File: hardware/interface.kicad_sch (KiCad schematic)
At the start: 0 parts

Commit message: Interface sheet: 2068 bus transceivers, gating, open-drain drivers, DMA drivers
- lib/tspico.kicad_sym: TS2068_Edge symbol (A1..A32/B1..B32, manual pin names)
- scripts/schlib.py: small KiCad schematic writer (stock symbols embedded
  verbatim, labels on pins, grid-snapped placement)
- scripts/gen_interface.py: P1, 4x 74LVC245, 74LVC04/08 gating, 74LVC07
  open-drain, 74LVC126 DMA drivers, 74LVC1G86 data direction, buttons,
  reset pull-down, EAR divider, decoupling
- Power decision: +5V from the edge only, USB is data only
- ERC: only cross-sheet labels remain (isolated/undriven until other sheets exist)

Co-Authored-By: Claude Fable 5.1 <noreply@anthropic.com>
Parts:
- added C1, C2, C3, C4, C5, C6, C7, C8: 100n, Capacitor_SMD:C_0603_1608Metric, symbol Device:C
- added P1: TS2068_Edge, tspico:TS2068_EdgeConnector_2x32, symbol tspico:TS2068_Edge
- added R1: 10k, Resistor_SMD:R_0603_1608Metric, symbol Device:R
- added R2: 4k7, Resistor_SMD:R_0603_1608Metric, symbol Device:R
- added R3: 1k, Resistor_SMD:R_0603_1608Metric, symbol Device:R
- added SW1: TS Reset, Button_Switch_SMD:SW_SPST_PTS645Sx43SMTR92, symbol Switch:SW_Push
- added SW2: NMI, Button_Switch_SMD:SW_SPST_PTS645Sx43SMTR92, symbol Switch:SW_Push
- added U1, U2, U3, U4: 74LVC245APW, Package_SO:TSSOP-20_4.4x6.5mm_P0.65mm, symbol 74xx:74LS245
- added U5: 74LVC04APW, Package_SO:TSSOP-14_4.4x5mm_P0.65mm, symbol 74xx:74LS04
- added U6: 74LVC08APW, Package_SO:TSSOP-14_4.4x5mm_P0.65mm, symbol 74xx:74LS08
- added U7: 74LVC07APW, Package_SO:TSSOP-14_4.4x5mm_P0.65mm, symbol 74xx:74LS07
- added U8: 74LVC126APW, Package_SO:TSSOP-14_4.4x5mm_P0.65mm, symbol 74xx:74LS126
- added U9: 74LVC1G86, Package_TO_SOT_SMD:SOT-23-5, symbol 74xGxx:74LVC1G86
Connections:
- new net +3V3: C1.1, C2.1, C3.1, C4.1, C5.1, C6.1, C7.1, C8.1, U1.20 (VCC), U2.20 (VCC), U3.20 (VCC), U4.20 (VCC), U5.14 (VCC), U6.14 (VCC), U7.13, U7.14 (VCC), U8.14 (VCC), U9.5 (VCC)
- new net +5V: P1.B4 (+5V)
- new net A0: P1.B10 (A0), U1.18 (B0)
- new net A1: P1.B11 (A1), U1.17 (B1)
- new net A10: P1.B19 (A10), U2.16 (B2)
- new net A11: P1.B18 (A11), U2.15 (B3)
- new net A12: P1.B17 (A12), U2.14 (B4)
- new net A13: P1.B16 (A13), U2.13 (B5)
- new net A14: P1.B15 (A14), U2.12 (B6), U4.13 (B5)
- new net A15: P1.B14 (A15), U2.11 (B7), U4.12 (B6)
- new net A2: P1.B12 (A2), U1.16 (B2)
- new net A3: P1.B13 (A3), U1.15 (B3)
- new net A4: P1.B25 (A4), U1.14 (B4)
- new net A5: P1.B24 (A5), U1.13 (B5)
- new net A6: P1.B23 (A6), U1.12 (B6)
- new net A7: P1.B22 (A7), U1.11 (B7)
- new net A8: P1.B21 (A8), U2.18 (B0)
- new net A9: P1.B20 (A9), U2.17 (B1)
- new net BUS_OWN: U6.12
- new net D0: P1.A7 (D0), U3.2 (A0)
- new net D1: P1.A8 (D1), U3.3 (A1)
- new net D2: P1.A9 (D2), U3.4 (A2)
- new net D3: P1.A12 (D3), U3.5 (A3)
- new net D4: P1.A13 (D4), U3.6 (A4)
- new net D5: P1.A11 (D5), U3.7 (A5)
- new net D6: P1.A10 (D6), U3.8 (A6)
- new net D7: P1.A4 (D7), U3.9 (A7)
- new net DATA_DIR: U3.1 (A->B), U9.4
- new net DMA_A14: U2.8 (A6)
- new net DMA_A15: U2.9 (A7)
- new net DMA_EN: U1.1 (A->B), U2.1 (A->B), U5.11, U8.1, U8.10, U8.4, U9.2
- new net EAR: P1.A2 (EAR), R2.2, R3.1
- new net GND: C1.2, C2.2, C3.2, C4.2, C5.2, C6.2, C7.2, C8.2, P1.A1 (GND), P1.A32 (GND), P1.B1 (GND), P1.B32 (GND), P1.B7 (PGND), P1.B8 (PGND), R1.2, R3.2, SW1.2, SW2.2, U1.10 (GND), U2.10 (GND), U3.10 (GND), U4.1 (A->B), U4.10 (GND), U4.19 (CE), U5.13, U5.7 (GND), U6.7 (GND), U7.7 (GND), U8.12, U8.13, U8.7 (GND), U9.3 (GND)
- new net IORQ_H: U5.4, U6.4
- new net IORQ_M1: U5.9, U6.6
- new net MA0: U1.2 (A0)
- new net MA1: U1.3 (A1)
- new net MA10: U2.4 (A2)
- new net MA11: U2.5 (A3)
- new net MA12: U2.6 (A4)
- new net MA13: U2.7 (A5)
- new net MA2: U1.4 (A2)
- new net MA3: U1.5 (A3)
- new net MA4: U1.6 (A4)
- new net MA5: U1.7 (A5)
- new net MA6: U1.8 (A6)
- new net MA7: U1.9 (A7)
- new net MA8: U2.2 (A0)
- new net MA9: U2.3 (A1)
- new net MD0: U3.18 (B0)
- new net MD1: U3.17 (B1)
- new net MD2: U3.16 (B2)
- new net MD3: U3.15 (B3)
- new net MD4: U3.14 (B4)
- new net MD5: U3.13 (B5)
- new net MD6: U3.12 (B6)
- new net MD7: U3.11 (B7)
- new net MREQ_H: U5.2, U6.1
- new net MREQ_RFSH: U5.5, U6.3
- new net RESET_REQ: R1.1, U7.11
- new net SOUND_2068: P1.A31 (SOUND)
- new net SPKR_TAPE: P1.B2 (SPKR_TAPE), U4.11 (B7)
- new net TAPE_IN: U4.9 (A7)
- new net TAPE_OUT: R2.1
- new net Z80_A14: U4.7 (A5)
- new net Z80_A15: U4.8 (A6)
- new net nBE: P1.A29 (~{BE}), U7.2
- new net nBE_G: U7.1
- new net nBUSAK: P1.A21 (~{BUSAK})
- new net nBUSRQ: P1.A23 (~{BUSRQ}), U7.6
- new net nBUSRQ_G: U7.5
- new net nDATA_OE: U3.19 (CE)
- new net nDMA_EN: U5.10, U6.13
- new net nDMA_MREQ: U6.8, U8.2
- new net nEXROM: P1.A27 (~{EXROM}), U4.15 (B3)
- new net nEXROM_L: U4.5 (A3)
- new net nINT: P1.A14 (~{INT}), U4.14 (B4)
- new net nINT_L: U4.6 (A4)
- new net nIORQ: P1.A18 (~{IORQ}), U5.3
- new net nIORQ_V: U5.8
- new net nM1: P1.A25 (~{M1}), U6.5
- new net nMRD: U6.9, U8.5
- new net nMREQ: P1.A17 (~{MREQ}), U5.1, U8.3
- new net nMREQ_V: U5.6
- new net nMWR: U6.10, U8.9
- new net nNMI: P1.A15 (~{NMI}), SW2.1, U7.8
- new net nNMI_G: U7.9
- new net nOE_ADDR: U1.19 (CE), U2.19 (CE), U6.11
- new net nRD: P1.A19 (~{RD}), U4.18 (B0), U8.6, U9.1
- new net nRD_L: U4.2 (A0)
- new net nRESET: P1.A24 (~{RESET}), SW1.1, U7.10
- new net nRFSH: P1.A26 (~{RFSH}), U6.2
- new net nROSCS: P1.A28 (~{ROSCS}), U4.16 (B2)
- new net nROSCS_L: U4.4 (A2)
- new net nWAIT: P1.A22 (~{WAIT}), U7.4
- new net nWAIT_G: U7.3
- new net nWR: P1.A20 (~{WR}), U4.17 (B1), U8.8
- new net nWR_L: U4.3 (A1)
- no-connect marks 0 -> 16
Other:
- note added: "Power: +5V from edge pin B4 only. +15V (B3) unused. USB is data only."
- note added: "R2/R3: TAPE_OUT (3.3 V) divided to about 0.6 V for the 2068 EAR input; values to be confirmed on the prototype."
- note added: "TS2068 bus interface. Nets: n = active low, _L = 3.3 V copy of a bus signal, _G = 3.3 V request driven onto the bus through an open-drain buffer."
- note removed: "Edge connector, address/data/control transceivers, open-drain drivers, reset, buttons, tape EAR/MIC dividers"

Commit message: Interface sheet: fix symbol text placement and layout overlaps
Co-Authored-By: Claude Fable 5.1 <noreply@anthropic.com>
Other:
- note added: "R2/R3: TAPE_OUT divided to ~0.6 V for the 2068 EAR input."
- note added: "Values to be confirmed on the prototype."
- note removed: "R2/R3: TAPE_OUT (3.3 V) divided to about 0.6 V for the 2068 EAR input; values to be confirmed on the prototype."

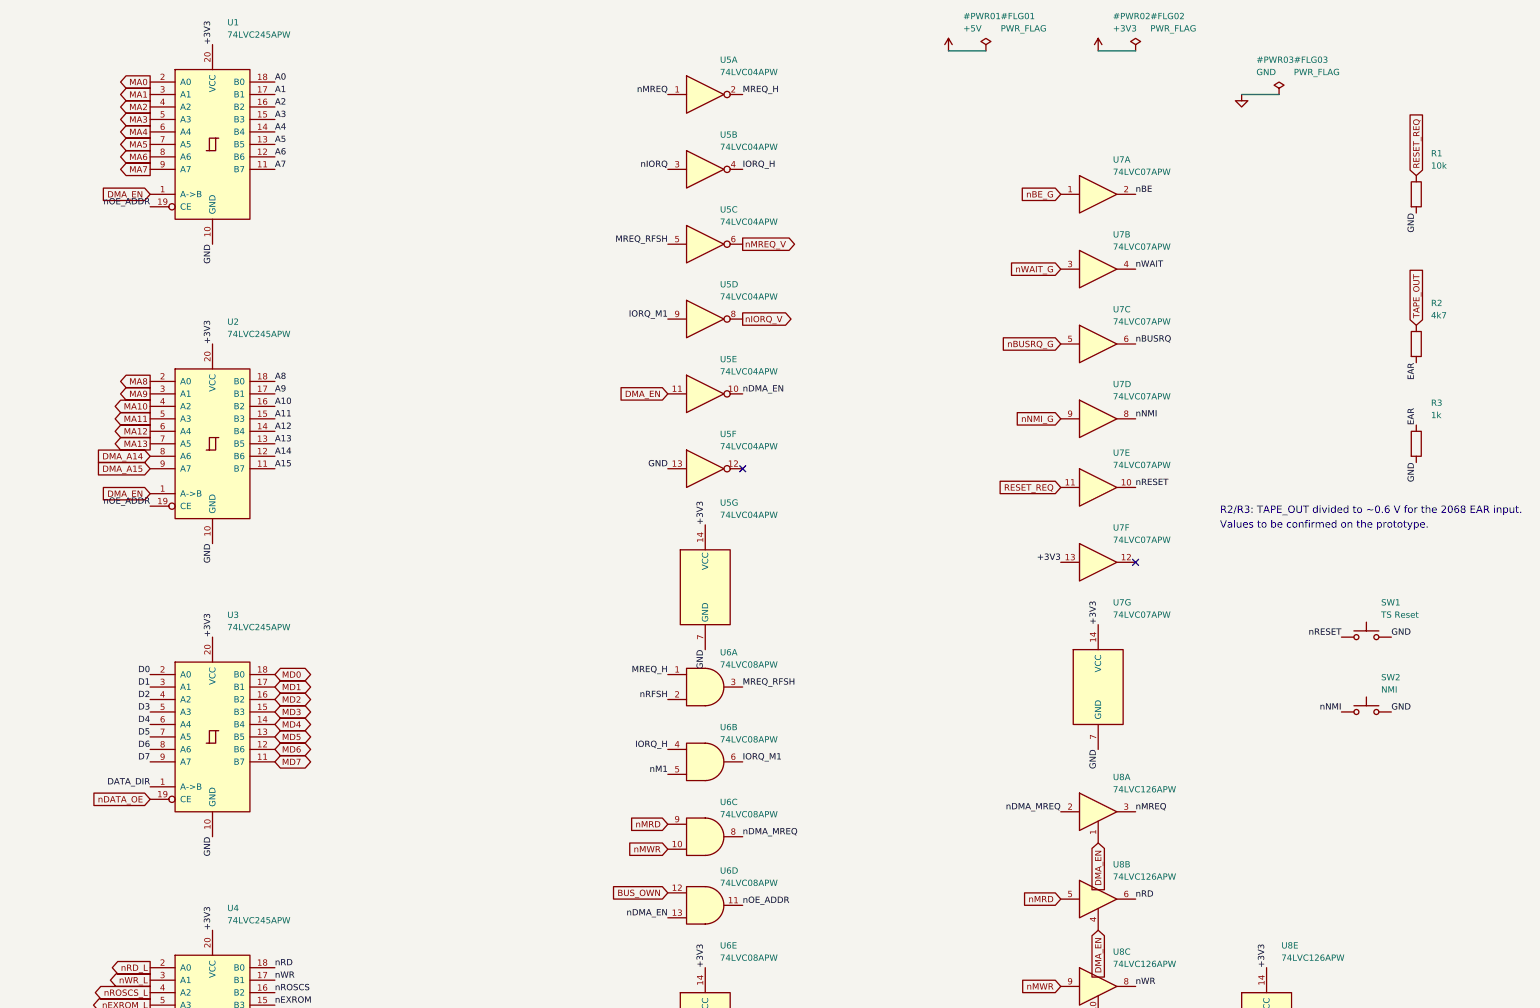
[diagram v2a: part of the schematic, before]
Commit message: Emulated memory: rewrite architecture, add local-bus/register sheet
- docs/v3-architecture.md: RP2350B serves DCK/ROM images from internal SRAM
  via PIO+DMA; no flash or SRAM chips; 8-bit multiplexed local bus; slot map
  file replaces fixed flash banks; ESP32-C3-WROOM-02 for Zimodem.
- memory sheet: 74LVC257 address byte muxes, ALO/AHI/CTL/STAT registers,
  74LVC139 select, power-on clear for CTL.
- interface sheet: 74LVC06 inverting open-drain drivers with active-high
  requests (safe power-up state), RESET_HOLD pull-up, address transceivers
  always enabled, MA8-MA15 to the muxes, WIFI_DL inverter.
- ERC: only cross-sheet labels/inputs pending the MCU and peripheral sheets.

Co-Authored-By: Claude Fable 5.1 <noreply@anthropic.com>
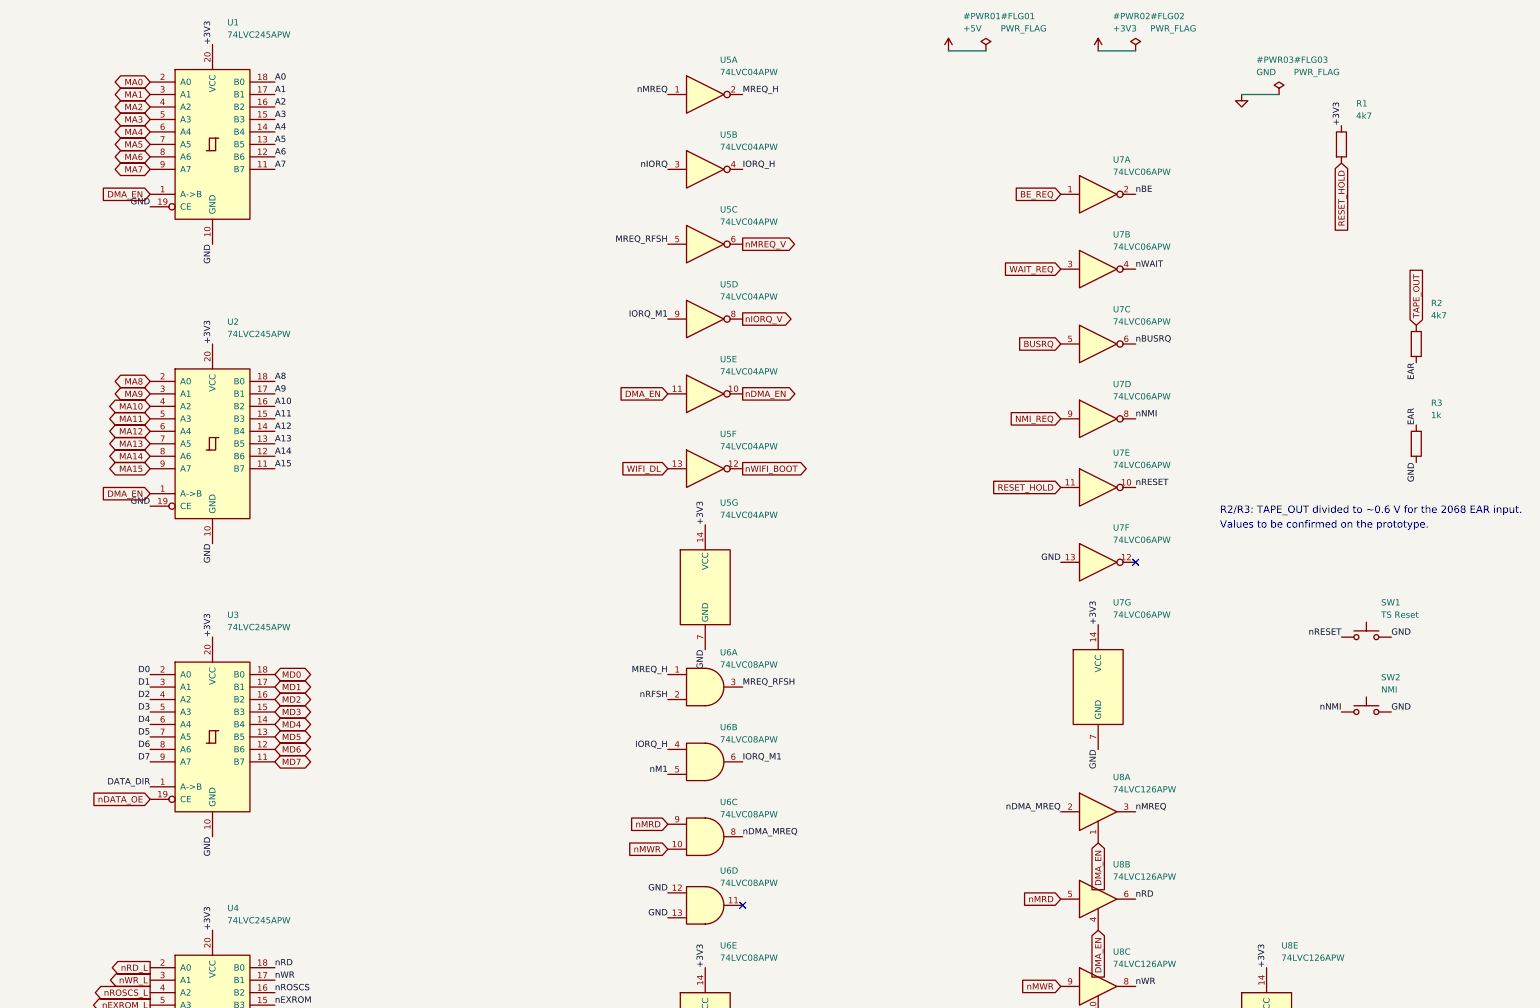
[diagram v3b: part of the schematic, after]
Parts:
- removed U7: 74LVC07APW, Package_SO:TSSOP-14_4.4x5mm_P0.65mm, symbol 74xx:74LS07
- added U7: 74LVC06APW, Package_SO:TSSOP-14_4.4x5mm_P0.65mm, symbol 74xx:74LS06
- R1: value 10k -> 4k7
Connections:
- net BUS_OWN is gone; now on net GND: U6.12
- net RESET_REQ is gone; now on net +3V3: R1.1
- net +3V3: now also U7.14 (VCC)
- net GND: now also U1.19 (CE), U2.19 (CE), U6.13, U7.13, U7.7 (GND); no longer R1.2, U5.13
- net nBE: now also U7.2
- net nBUSRQ: now also U7.6
- net nDMA_EN: no longer U6.13
- net nNMI: now also U7.8
- net nRESET: now also U7.10
- net nWAIT: now also U7.4
- net nWIFI_BOOT: now reaches U5.12
- net DMA_A14 renamed MA14
- net DMA_A15 renamed MA15
- removed net nOE_ADDR: U1.19 (CE), U2.19 (CE), U6.11
- new net BE_REQ: U7.1
- new net BUSRQ: U7.5
- new net NMI_REQ: U7.9
- new net RESET_HOLD: R1.2, U7.11
- new net WAIT_REQ: U7.3
- new net WIFI_DL: U5.13

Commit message: Remaining sheets: power, SD and display, WiFi, audio, joystick; ERC clean
- Power: Schottky diode-OR of edge +5V and USB VBUS (card runs from the
  2068/expansion bus, USB alone, or both), two TLV1117LV33 LDOs, bulk caps
- SD: Hirose DM3AT in SPI mode with series R, pull-ups, card detect to STAT
- OLED: 7-pin header (Waveshare 1.27in 128x96 SSD1351) on SPI1
- WiFi: ESP32-C3-WROOM-02 on UART, EN/boot from CTL, IO8 pull-up
- Audio: PWM low-pass, 2068 SOUND mix, MCP6002 buffers, 3.5 mm jack
- Joystick: DE-9 Kempston with pull-ups, series R, optional +5V jumper
- Memory sheet: activity LED on CTL bit 6
- Docs: power decision updated

Co-Authored-By: Claude Fable 5.1 <noreply@anthropic.com>
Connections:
- net +5V renamed +5V_EDGE
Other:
- note added: "Power: edge +5V (B4) goes to the power sheet as +5V_EDGE and is diode-ORed with USB VBUS. +15V (B3) unused."
- note removed: "Power: +5V from edge pin B4 only. +15V (B3) unused. USB is data only."
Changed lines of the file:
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@@
   (title_block (title "TS-Pico v3: 2068 Interface") (rev "0.1") (company "Timex/Sinclair Online User Group"))
   (text "TS2068 bus interface. Nets: n = active low, _L = 3.3 V copy of a bus signal, _G = 3.3 V request driven onto the bus through an open-drain buffer." (exclude_from_sim no) (at 20 285 0) (effects (font (size 2.5 2.5)) (justify left bottom)))
-  (text "Power: +5V from edge pin B4 only. +15V (B3) unused. USB is data only." (exclude_from_sim no) (at 20 290 0) (effects (font (size 2.0 2.0)) (justify left bottom)))
+  (text "Power: edge +5V (B4) goes to the power sheet as +5V_EDGE and is diode-ORed with USB VBUS. +15V (B3) unused." (exclude_from_sim no) (at 20 290 0) (effects (font (size 2.0 2.0)) (justify left bottom)))
   (symbol (lib_id "tspico:TS2068_Edge") (at 59.69 119.38 0) (unit 1)
     (exclude_from_sim no) (in_bom yes) (on_board yes) (dnp no)
@@
   (label "GND" (at 77.47 95.25 0) (effects (font (size 1.27 1.27)) (justify left bottom)))
   (label "GND" (at 77.47 97.79 0) (effects (font (size 1.27 1.27)) (justify left bottom)))
-  (label "+5V" (at 77.47 87.63 0) (effects (font (size 1.27 1.27)) (justify left bottom)))
+  (global_label "+5V_EDGE" (shape output) (at 77.47 87.63 0) (effects (font (size 1.27 1.27)) (justify left)))
   (label "EAR" (at 41.91 82.55 180) (effects (font (size 1.27 1.27)) (justify right bottom)))
   (label "SPKR_TAPE" (at 77.47 82.55 0) (effects (font (size 1.27 1.27)) (justify left bottom)))
@@
   (no_connect (at 77.47 153.67))
   (no_connect (at 77.47 156.21))
-  (symbol (lib_id "power:+5V") (at 299.72 30.48 0) (unit 1)
-    (exclude_from_sim no) (in_bom yes) (on_board yes) (dnp no)
-    (property "Reference" "#PWR01" (at 302.72 23.44 0) (effects (font (size 1.27 1.27)) (justify left)))
-    (property "Value" "+5V" (at 302.72 25.94 0) (effects (font (size 1.27 1.27)) (justify left)))
-    (property "Footprint" "" (at 299.72 30.48 0) (effects (font (size 1.27 1.27)) (justify left) (hide yes)))
-    (property "Datasheet" "" (at 299.72 30.48 0) (effects (font (size 1.27 1.27)) (justify left) (hide yes)))
-    (property "Description" "" (at 299.72 30.48 0) (effects (font (size 1.27 1.27)) (justify left) (hide yes)))
-    (pin "1")
-    (instances (project "tspico-v3" (path "/9088d141-8624-4d5c-91a9-7a3a7a90b3cc/a611a6fb-5e55-4c31-9c90-ae90d05d13a4" (reference "#PWR01") (unit 1))))
-  )
-  (symbol (lib_id "power:PWR_FLAG") (at 307.34 30.48 0) (unit 1)
-    (exclude_from_sim no) (in_bom yes) (on_board yes) (dnp no)
-    (property "Reference" "#FLG01" (at 310.34 23.44 0) (effects (font (size 1.27 1.27)) (justify left)))
-    (property "Value" "PWR_FLAG" (at 310.34 25.94 0) (effects (font (size 1.27 1.27)) (justify left)))
-    (property "Footprint" "" (at 307.34 30.48 0) (effects (font (size 1.27 1.27)) (justify left) (hide yes)))
-    (property "Datasheet" "" (at 307.34 30.48 0) (effects (font (size 1.27 1.27)) (justify left) (hide yes)))
-    (property "Description" "" (at 307.34 30.48 0) (effects (font (size 1.27 1.27)) (justify left) (hide yes)))
-    (pin "1")
-    (instances (project "tspico-v3" (path "/9088d141-8624-4d5c-91a9-7a3a7a90b3cc/a611a6fb-5e55-4c31-9c90-ae90d05d13a4" (reference "#FLG01") (unit 1))))
-  )
-  (wire (pts (xy 299.72 30.48) (xy 307.34 30.48)) (stroke (width 0) (type default)))
   (symbol (lib_id "power:+3V3") (at 330.2 30.48 0) (unit 1)
     (exclude_from_sim no) (in_bom yes) (on_board yes) (dnp no)
@@
     (instances (project "tspico-v3" (path "/9088d141-8624-4d5c-91a9-7a3a7a90b3cc/a611a6fb-5e55-4c31-9c90-ae90d05d13a4" (reference "#PWR02") (unit 1))))
   )
-  (symbol (lib_id "power:PWR_FLAG") (at 337.82 30.48 0) (unit 1)
-    (exclude_from_sim no) (in_bom yes) (on_board yes) (dnp no)
-    (property "Reference" "#FLG02" (at 340.82 23.44 0) (effects (font (size 1.27 1.27)) (justify left)))
-    (property "Value" "PWR_FLAG" (at 340.82 25.94 0) (effects (font (size 1.27 1.27)) (justify left)))
-    (property "Footprint" "" (at 337.82 30.48 0) (effects (font (size 1.27 1.27)) (justify left) (hide yes)))
-    (property "Datasheet" "" (at 337.82 30.48 0) (effects (font (size 1.27 1.27)) (justify left) (hide yes)))
-    (property "Description" "" (at 337.82 30.48 0) (effects (font (size 1.27 1.27)) (justify left) (hide yes)))
-    (pin "1")
-    (instances (project "tspico-v3" (path "/9088d141-8624-4d5c-91a9-7a3a7a90b3cc/a611a6fb-5e55-4c31-9c90-ae90d05d13a4" (reference "#FLG02") (unit 1))))
-  )
-  (wire (pts (xy 330.20 30.48) (xy 337.82 30.48)) (stroke (width 0) (type default)))
+  (label "+3V3" (at 330.20 30.48 270) (effects (font (size 1.27 1.27)) (justify right bottom)))
   (symbol (lib_id "power:GND") (at 359.41 39.37 0) (unit 1)
     (exclude_from_sim no) (in_bom yes) (on_board yes) (dnp no)
@@
     (instances (project "tspico-v3" (path "/9088d141-8624-4d5c-91a9-7a3a7a90b3cc/a611a6fb-5e55-4c31-9c90-ae90d05d13a4" (reference "#PWR03") (unit 1))))
   )
-  (symbol (lib_id "power:PWR_FLAG") (at 367.03 39.37 0) (unit 1)
-    (exclude_from_sim no) (in_bom yes) (on_board yes) (dnp no)
-    (property "Reference" "#FLG03" (at 370.03 32.33 0) (effects (font (size 1.27 1.27)) (justify left)))
-    (property "Value" "PWR_FLAG" (at 370.03 34.83 0) (effects (font (size 1.27 1.27)) (justify left)))
-    (property "Footprint" "" (at 367.03 39.37 0) (effects (font (size 1.27 1.27)) (justify left) (hide yes)))
-    (property "Datasheet" "" (at 367.03 39.37 0) (effects (font (size 1.27 1.27)) (justify left) (hide yes)))
-    (property "Description" "" (at 367.03 39.37 0) (effects (font (size 1.27 1.27)) (justify left) (hide yes)))
-    (pin "1")
-    (instances (project "tspico-v3" (path "/9088d141-8624-4d5c-91a9-7a3a7a90b3cc/a611a6fb-5e55-4c31-9c90-ae90d05d13a4" (reference "#FLG03") (unit 1))))
-  )
-  (wire (pts (xy 359.41 39.37) (xy 367.03 39.37)) (stroke (width 0) (type default)))
+  (label "GND" (at 359.41 39.37 90) (effects (font (size 1.27 1.27)) (justify left bottom)))
   (symbol (lib_id "74xx:74LS245") (at 149.86 49.53 0) (unit 1)
     (exclude_from_sim no) (in_bom yes) (on_board yes) (dnp no)

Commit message: BOM pass: LCSC and MPN fields on every part, JLCPCB BOM export
- scripts/parts.py: part table looked up 2026-09-16; schlib stamps fields
- substitutions for stock: 74HC273PW, 74LVC139PW, TI LVC04/08/126/574/1G86,
  33R USB series, XKB TS-1187A switches, Panasonic polymer 220uF, B5819W
- bom/: JLCPCB-format and full BOM CSVs

Co-Authored-By: Claude Fable 5.1 <noreply@anthropic.com>
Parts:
- C1, C2, C3, C4, C5, C6, C7, C8: LCSC (none) -> C14663; MPN (none) -> CC0603KRX7R9BB104
- R1, R2: LCSC (none) -> C23162; MPN (none) -> 0603WAF4701T5E
- R3: LCSC (none) -> C21190; MPN (none) -> 0603WAF1001T5E
- SW1, SW2: footprint Button_Switch_SMD:SW_SPST_PTS645Sx43SMTR92 -> Button_Switch_SMD:SW_Push_1P1T_XKB_TS-1187A; LCSC (none) -> C318884; MPN (none) -> TS-1187A-B-A-B
- U1, U2, U3, U4: LCSC (none) -> C6082; MPN (none) -> 74LVC245APW,118
- U5: LCSC (none) -> C7806; MPN (none) -> SN74LVC04APWRG4
- U6: LCSC (none) -> C465737; MPN (none) -> SN74LVC08APWR
- U7: LCSC (none) -> C131311; MPN (none) -> 74LVC06APW,118
- U8: LCSC (none) -> C7815; MPN (none) -> SN74LVC126APWR
- U9: LCSC (none) -> C402161; MPN (none) -> SN74LVC1G86DBVR
